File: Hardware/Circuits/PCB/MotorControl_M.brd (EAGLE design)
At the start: 74.8 x 147 mm, 77 parts, among them IC1 74AHC1G125FDBV, P1 M-2X10-87759, U1 MIC2005, U3 74HC4051BQ, U4 74HC4051BQ

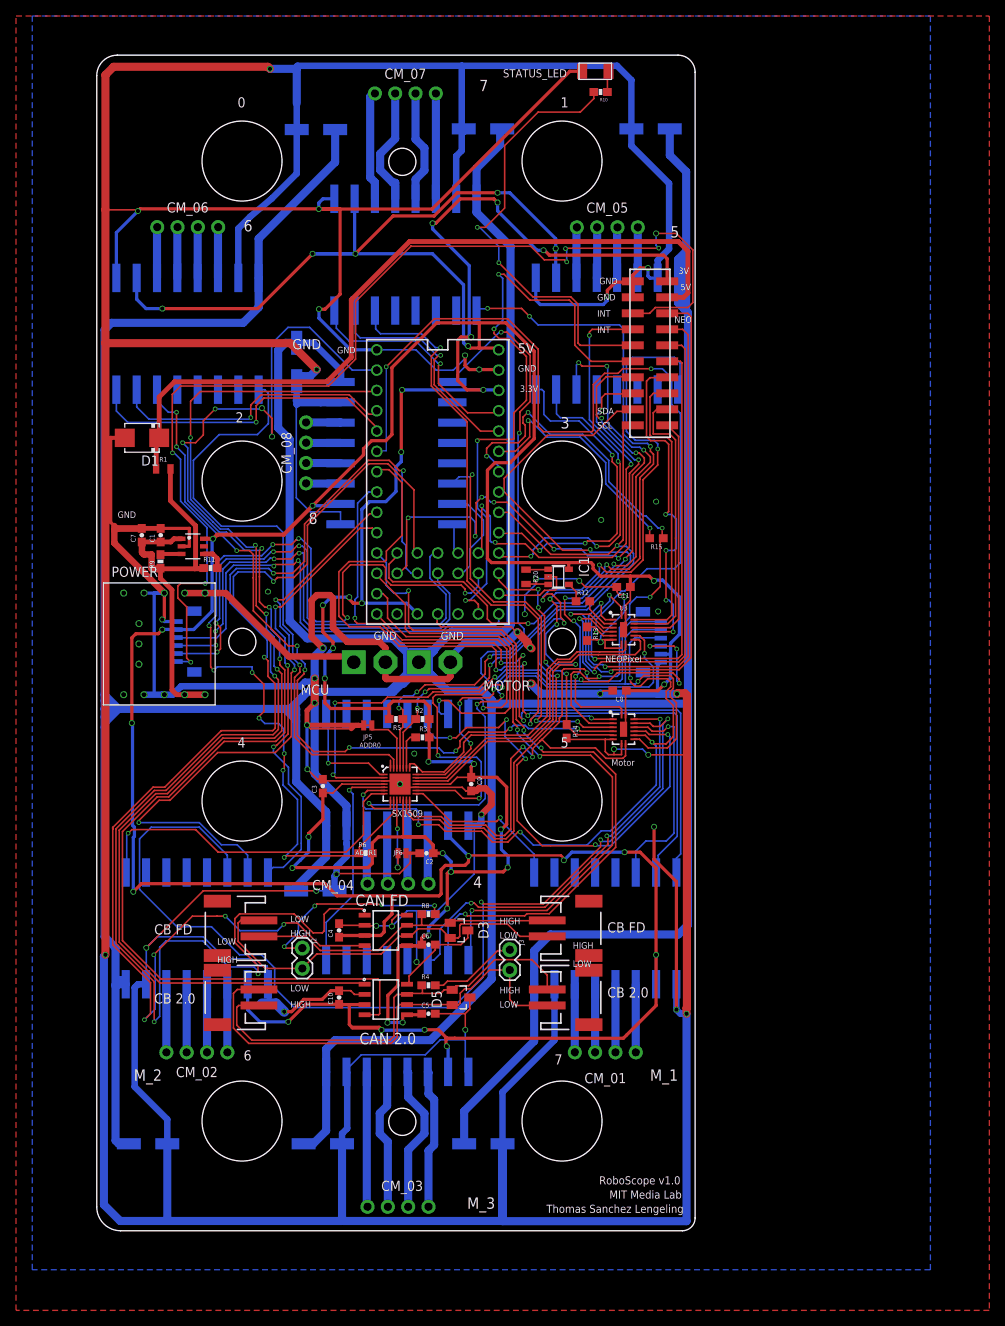
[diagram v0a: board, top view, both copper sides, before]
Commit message: clean traces and silscreen
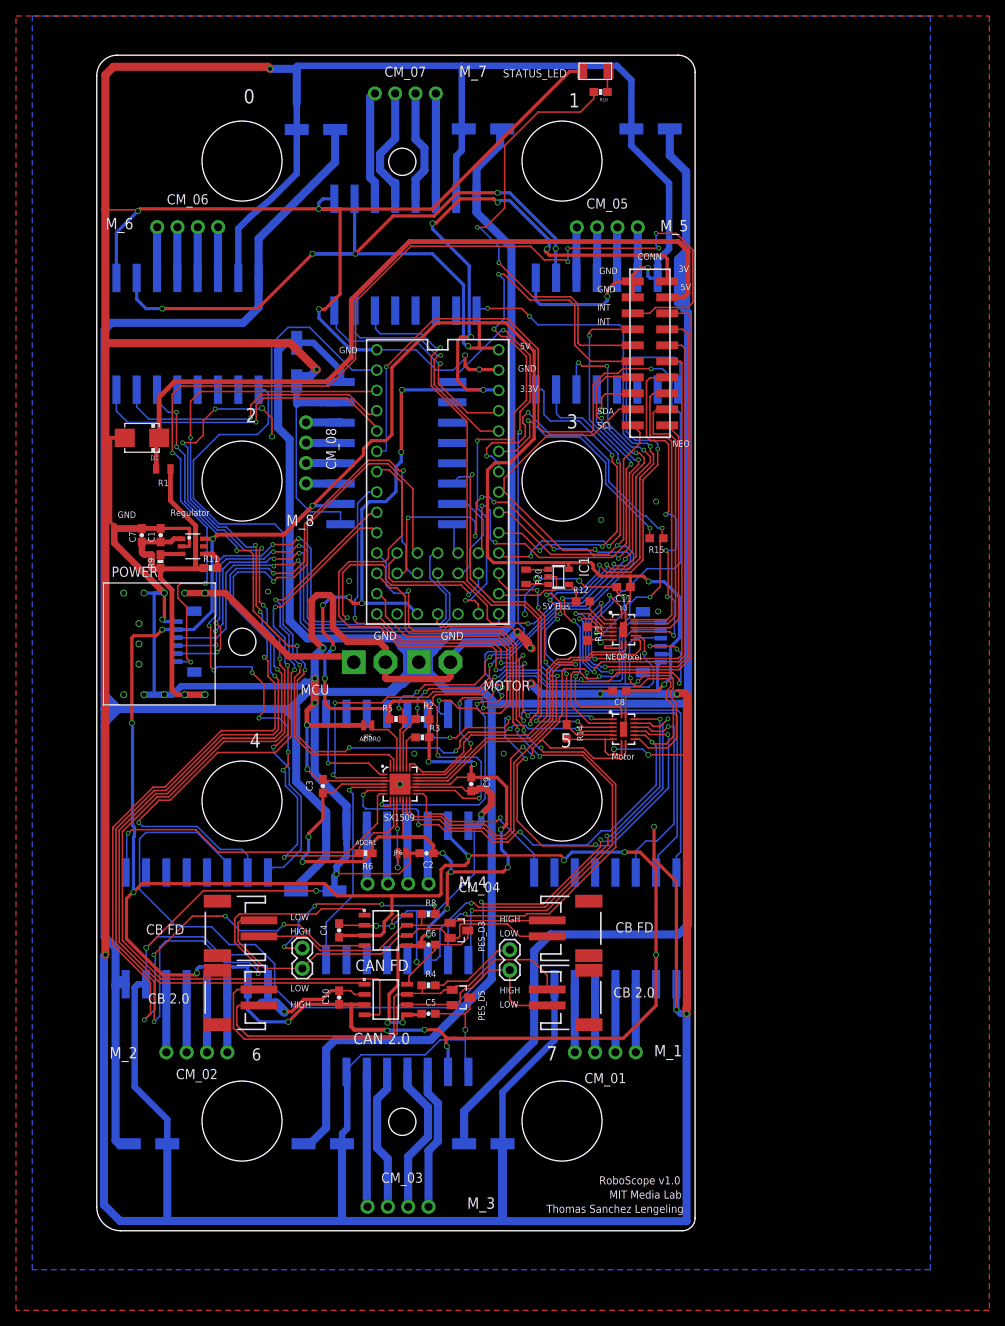
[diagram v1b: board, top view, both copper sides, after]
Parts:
- renumbered D3 to PES_D3, D5 to PES_D5
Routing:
- net VCC_5VREG: track 491.1 -> 517.4 mm, vias 21 -> 22
- net VCC_M: track 693.3 -> 703.1 mm
- net GND_MCU: track 1240.2 -> 1233.3 mm, vias 46 -> 48
- net SX00_8: track 110.7 -> 106.8 mm
- net SX00_7: track 85.3 -> 81.7 mm
- net CAN_TX3: track 167.5 -> 164.5 mm
- net 3.3V: track 285.5 -> 282.9 mm
- net INT_00: track 120.5 -> 122.4 mm
- net SX00_SDA: track 82.0 -> 83.2 mm
- net NEOPIXEL_08_5V: track 73.7 -> 72.5 mm
- net SX00_10: track 20.8 -> 21.9 mm
- net MOTOR_TX_04: track 62.3 -> 63.3 mm
- net NEOPIXEL_04_5V: track 44.1 -> 45.0 mm
- net MOTOR_TX_02: track 126.3 -> 125.5 mm
- net MSTEP_03: track 90.6 -> 89.8 mm
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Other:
- board text added: "5V Bus"
- board text added: "CONN"
- board text added: "M_4"
- board text added: "M_5"
- board text added: "M_6"
- board text added: "M_7"
- board text added: "M_8"
- board text added: "Regulator"

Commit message: pcbs
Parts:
- added C12, C13, C14, C15, C16, C17, C18, C19: (no value), we-rcl:C1210
- added D2, D3, D4, D5, D6, D7, D8, D9: (no value), we-rcl:SOD123
- R15: value 10k -> 1k
- R4: value 120Ohms -> 120
- moved DRILEGEND 126.8 mm to (-1.69, 117.9)
- moved R14 0.26 mm to (58.9, 67.8)
- turned R15 to 0 degrees
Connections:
- removed net MOTOR_TX_01: MOTOR_01.STBY, U4.13
- removed net MOTOR_TX_02: MOTOR_02.STBY, U4.14
- removed net MOTOR_TX_03: MOTOR_03.STBY, U4.15
- removed net MOTOR_TX_04: MOTOR_04.STBY, U4.12
- removed net MOTOR_TX_05: MOTOR_05.STBY, U4.1
- removed net MOTOR_TX_06: MOTOR_06.STBY, U4.5
- removed net MOTOR_TX_07: MOTOR_07.STBY, U4.2
- removed net MOTOR_TX_08: MOTOR_08.STBY, U4.4
- new net MOTOR_TX_RX_01: MOTOR_01.1, U4.13
- new net MOTOR_TX_RX_02: MOTOR_02.1, U4.14
- new net MOTOR_TX_RX_03: MOTOR_03.1, U4.15
- new net MOTOR_TX_RX_04: MOTOR_04.1, U4.12
- new net MOTOR_TX_RX_05: MOTOR_05.1, U4.1
- new net MOTOR_TX_RX_06: MOTOR_06.1, U4.5
- new net MOTOR_TX_RX_07: MOTOR_07.1, U4.2
- new net MOTOR_TX_RX_08: MOTOR_08.1, U4.4
- net GND_MCU: now also C12.1, C13.1, C14.1, C15.1, C16.1, C17.1, C18.1, C19.1
- net INPUT_01: no longer J1.6
- net MOTOR_MUX_RX: now also R15.1, U4.3; no longer R15.2
- net MOTOR_MUX_TX: now also R15.2; no longer R15.1, U4.3
- net SX00_1: now also J1.6
- net VCC_5VREG: now also D2.A, D3.A, D4.A, D5.A, D6.A, D7.A, D8.A, D9.A
- net VCC_M: now also C12.2, C13.2, C14.2, C15.2, C16.2, C17.2, C18.2, C19.2, D2.C, D3.C, D4.C, D5.C, D6.C, D7.C, D8.C, D9.C
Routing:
- net INPUT_01: track 138.6 -> 0.00 mm, vias 7 -> 0
- net MOTOR_TX_02: track 125.5 -> 0.00 mm, vias 3 -> 0
- net GND_MCU: track 1233.3 -> 1357.1 mm, vias 48 -> 53
- net MOTOR_TX_RX_02: track 0.00 -> 101.0 mm, vias 0 -> 3
- net MOTOR_TX_06: track 96.9 -> 0.00 mm, vias 9 -> 0
- net MOTOR_TX_RX_06: track 0.00 -> 95.7 mm, vias 0 -> 9
- net MOTOR_TX_07: track 78.5 -> 0.00 mm, vias 3 -> 0
- net MOTOR_TX_RX_07: track 0.00 -> 73.5 mm, vias 0 -> 3
- net MOTOR_TX_05: track 67.5 -> 0.00 mm, vias 7 -> 0
- net MOTOR_TX_RX_04: track 0.00 -> 67.2 mm, vias 0 -> 5
- net VCC_M: track 703.1 -> 768.0 mm
- net VCC_5VREG: track 517.4 -> 581.0 mm, vias 22 -> 23
- net MOTOR_TX_04: track 63.3 -> 0.00 mm, vias 5 -> 0
- net MOTOR_TX_RX_03: track 0.00 -> 62.2 mm, vias 0 -> 3
- net MOTOR_TX_RX_05: track 0.00 -> 56.7 mm, vias 0 -> 5
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
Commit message: update circuits
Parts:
- added J5: (no value), SparkFun-Connectors:1X01
- moved R15 0.08 mm to (70.0, 91.9)
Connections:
- net INPUT_01: now also J5.1
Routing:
- net INPUT_01: track 0.00 -> 123.2 mm, vias 0 -> 10
- net GND_MCU: track 1357.1 -> 1347.1 mm
- net SX00_12: track 105.3 -> 101.4 mm
- net INT_00: track 120.9 -> 118.5 mm
- net MOTOR_TX_RX_07: track 73.5 -> 71.4 mm
- net INT_01: track 68.4 -> 69.9 mm
- net SX00_9: track 72.6 -> 71.4 mm
- net MOTOR_TX_RX_08: track 53.5 -> 54.6 mm
- net MOTOR_TX_RX_04: track 67.2 -> 66.2 mm
- net CAN_RX3: track 157.7 -> 156.8 mm
- net NEOPIXEL_05_5V: track 61.9 -> 61.1 mm
- net NEOPIXEL_07_5V: track 67.4 -> 66.6 mm
- net SX00_0: track 76.0 -> 75.2 mm
- net CAN_TX3: track 163.7 -> 163.0 mm
- net SX00_13: track 40.4 -> 41.0 mm
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
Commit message: update motors
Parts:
- removed IC1: 74AHC1G125FDBV, 74xx-little-us:SOT23-5
- removed U3: 74HC4051BQ, 8mux:DHVQFN-16-2.5X3.5MM
- added D10: SOD123L, we-rcl:SOD123
- added R16, R17, R18, R19, R7: 100, SparkFun-Resistors:0603
- added U2: 74HCT245D,65220-TSSOP, 74HCT245D_652:20-TSSOP
- C11: value 0.1uF -> 1uf; device SparkFun-Capacitors:0603 -> SparkFun-Capacitors:0603-CAP
- C12: value (none) -> 10uf
- MOTOR_01, MOTOR_02, MOTOR_03, MOTOR_04, MOTOR_05, MOTOR_06, MOTOR_07, MOTOR_08: value DRV8880 -> DRV8880TMC2209; device STSPIN220:DRV8880 -> STSPIN220:TMC2209_SMD
- R13: value 10K -> 100
- R20: value 10K -> 100; device SparkFun-Resistors:0805 -> SparkFun-Resistors:0603
- moved DRILEGEND 89.1 mm to (-89.1, 100.4)
- moved R20 20.5 mm to (71.3, 76.8), turned to 0 degrees
- moved R13 10.7 mm to (70.8, 84.8), turned to 0 degrees
- moved R12 9.91 mm to (70.3, 86.5)
- moved MOTOR_04 1.78 mm to (37.5, 61.2)
- moved CM_04 1.40 mm to (37.6, 47.4)
- moved C11 1.37 mm to (64.5, 86.4)
- moved D5 1.28 mm to (34.7, 61.7)
- moved C19 1.27 mm to (31.8, 62.0)
- moved MOTOR_07 1.25 mm to (37.6, 126.6)
- moved D2 0.56 mm to (6.30, 44.4)
- moved CM_06 0.51 mm to (11.3, 131.3)
- moved MOTOR_08 0.51 mm to (37.9, 102.6)
- moved C12 0.38 mm to (3.68, 44.5)
- moved POWER_M 0.27 mm to (42.1, 76.2)
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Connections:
- removed net INT_03: P1.14, U$3.25
- removed net LIMIT_01: J1.3, U$3.13
- removed net LIMIT_02: J1.4, U$3.28
- removed net LIMIT_03: J1.5, U$3.29
- removed net MOTOR_MUX_E: R14.1, U$3.15/A1, U4.6
- removed net N$4: R12.2, U3.3
- removed net NEO_5V_Z: IC1.4, R12.1
- removed net NEO_MUX_E: R13.1, U$3.4, U3.6
- removed net NEO_TX3: IC1.2, U$3.14/A0
- new net INPUT_02: J4.3, P1.14
- new net N$11: R16.1, U2.15
- new net N$14: R18.1, U2.13
- new net N$15: R19.1, U2.12
- new net N$16: R20.1, U2.11
- new net N$5: D10.C, U$3.VIN
- new net N$6: R7.1, U2.18
- new net N$8: R12.1, U2.17
- new net N$9: R13.1, U2.16
- new net NEOPIXEL_01_3V: U$3.4, U2.2
- new net NEOPIXEL_02_3V: U$3.13, U2.3
- new net NEOPIXEL_03_3V: U$3.14/A0, U2.4
- new net NEOPIXEL_04_3V: U$3.15/A1, U2.5
- new net NEOPIXEL_05_3V: U$3.24, U2.6
- new net NEOPIXEL_06_3V: U$3.25, U2.7
- new net NEOPIXEL_07_3V: U$3.28, U2.8
- new net NEOPIXEL_08_3V: U$3.29, U2.9
- net GND_MCU: now also U2.10, U2.19; no longer IC1.3, R13.2, R20.2, U3.7, U3.8
- net INT_00: no longer U$3.24
- net MOTOR_TX_RX_01: now also MOTOR_01.TX/RX; no longer MOTOR_01.1
- net MOTOR_TX_RX_02: now also MOTOR_02.TX/RX; no longer MOTOR_02.1
- net MOTOR_TX_RX_03: now also MOTOR_03.TX/RX; no longer MOTOR_03.1
- net MOTOR_TX_RX_04: now also MOTOR_04.TX/RX; no longer MOTOR_04.1
- net MOTOR_TX_RX_05: now also MOTOR_05.TX/RX; no longer MOTOR_05.1
- net MOTOR_TX_RX_06: now also MOTOR_06.TX/RX; no longer MOTOR_06.1
- net MOTOR_TX_RX_07: now also MOTOR_07.TX/RX; no longer MOTOR_07.1
- net MOTOR_TX_RX_08: now also MOTOR_08.TX/RX; no longer MOTOR_08.1
- net N$12: now also R17.1, U2.14; no longer IC1.1, R20.1
- net NEOPIXEL_01_5V: now also R7.2; no longer U3.13
- net NEOPIXEL_02_5V: now also R12.2; no longer U3.14
- net NEOPIXEL_03_5V: now also R13.2; no longer U3.15
- net NEOPIXEL_04_5V: now also R16.2; no longer U3.12
- net NEOPIXEL_05_5V: now also R17.2; no longer U3.1
- net NEOPIXEL_06_5V: now also R18.2; no longer U3.5
- net NEOPIXEL_07_5V: now also R19.2; no longer U3.2
- net NEOPIXEL_08_5V: now also R20.2; no longer U3.4
- net SX00_1: now also J1.3; no longer J1.6
- net SX00_11: now also R14.1, U4.6; no longer U3.11
- net SX00_13: now also J1.5; no longer U3.10
- net SX00_15: now also J1.6; no longer U3.9
- net SX00_3: now also J1.4; no longer J4.3
- net VCC_5VREG: now also D10.A, MOTOR_01.5V, MOTOR_02.5V, MOTOR_03.5V, MOTOR_04.5V, MOTOR_05.5V, MOTOR_06.5V, MOTOR_07.5V, MOTOR_08.5V, U2.1, U2.20; no longer IC1.5, MOTOR_01.FAULT, MOTOR_02.FAULT, MOTOR_03.FAULT, MOTOR_04.FAULT, MOTOR_05.FAULT, MOTOR_06.FAULT, MOTOR_07.FAULT, MOTOR_08.FAULT, U$3.VIN, U3.16, U3.EP
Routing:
- net NEO_MUX_E: track 110.8 -> 0.00 mm, vias 3 -> 0
- net INT_00: track 118.5 -> 10.0 mm, vias 11 -> 0
- net LIMIT_03: track 64.2 -> 0.00 mm, vias 4 -> 0
- net INT_03: track 63.8 -> 0.00 mm, vias 4 -> 0
- net LIMIT_02: track 59.6 -> 0.00 mm, vias 4 -> 0
- net LIMIT_01: track 57.8 -> 0.00 mm, vias 2 -> 0
- net INPUT_02: track 0.00 -> 57.2 mm, vias 0 -> 1
- net VCC_5VREG: track 580.5 -> 633.6 mm
- net NEOPIXEL_01_3V: track 0.00 -> 47.1 mm, vias 0 -> 6
- net GND_MCU: track 1347.1 -> 1300.7 mm, vias 53 -> 54
- net VCC_M: track 768.0 -> 804.4 mm
- net SX00_3: track 72.3 -> 39.9 mm, vias 7 -> 5
- net MOTOR_MUX_E: track 32.3 -> 0.00 mm, vias 4 -> 0
- net NEOPIXEL_08_3V: track 0.00 -> 31.5 mm, vias 0 -> 4
- net SX00_11: track 63.7 -> 35.7 mm
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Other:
- board text removed: "01-16"
- board text removed: "LAYER-STACK"
